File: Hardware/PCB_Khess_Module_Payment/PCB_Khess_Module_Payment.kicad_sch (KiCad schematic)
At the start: 50 parts, among them IC1 SI4435DDY-T1-GE3, IC2 MCP73844-840I_MS, J1 Conn_02x20_Odd_Even, J2 Conn_01x02, J3 Conn_01x08, J4 Conn_01x04, J6 Conn_01x08, J7 694001, U2 FSV330AF, U3 171013801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

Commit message: review schematics
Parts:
- removed U4: LM393, symbol Comparator:LM393
- added U1: MCP6001-OT, Package_TO_SOT_SMD:SOT-23-5, symbol Amplifier_Operational:MCP6001-OT
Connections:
- net +3.3V: now also U1.5 (V+)
- net Batterie_Faible_GPIO: now also U1.1
- net GND: now also U1.2 (V-)
- net Niveau_Batterie: now also U1.3 (+)
- net at R7.2, R8.1: now also U1.4 (-)

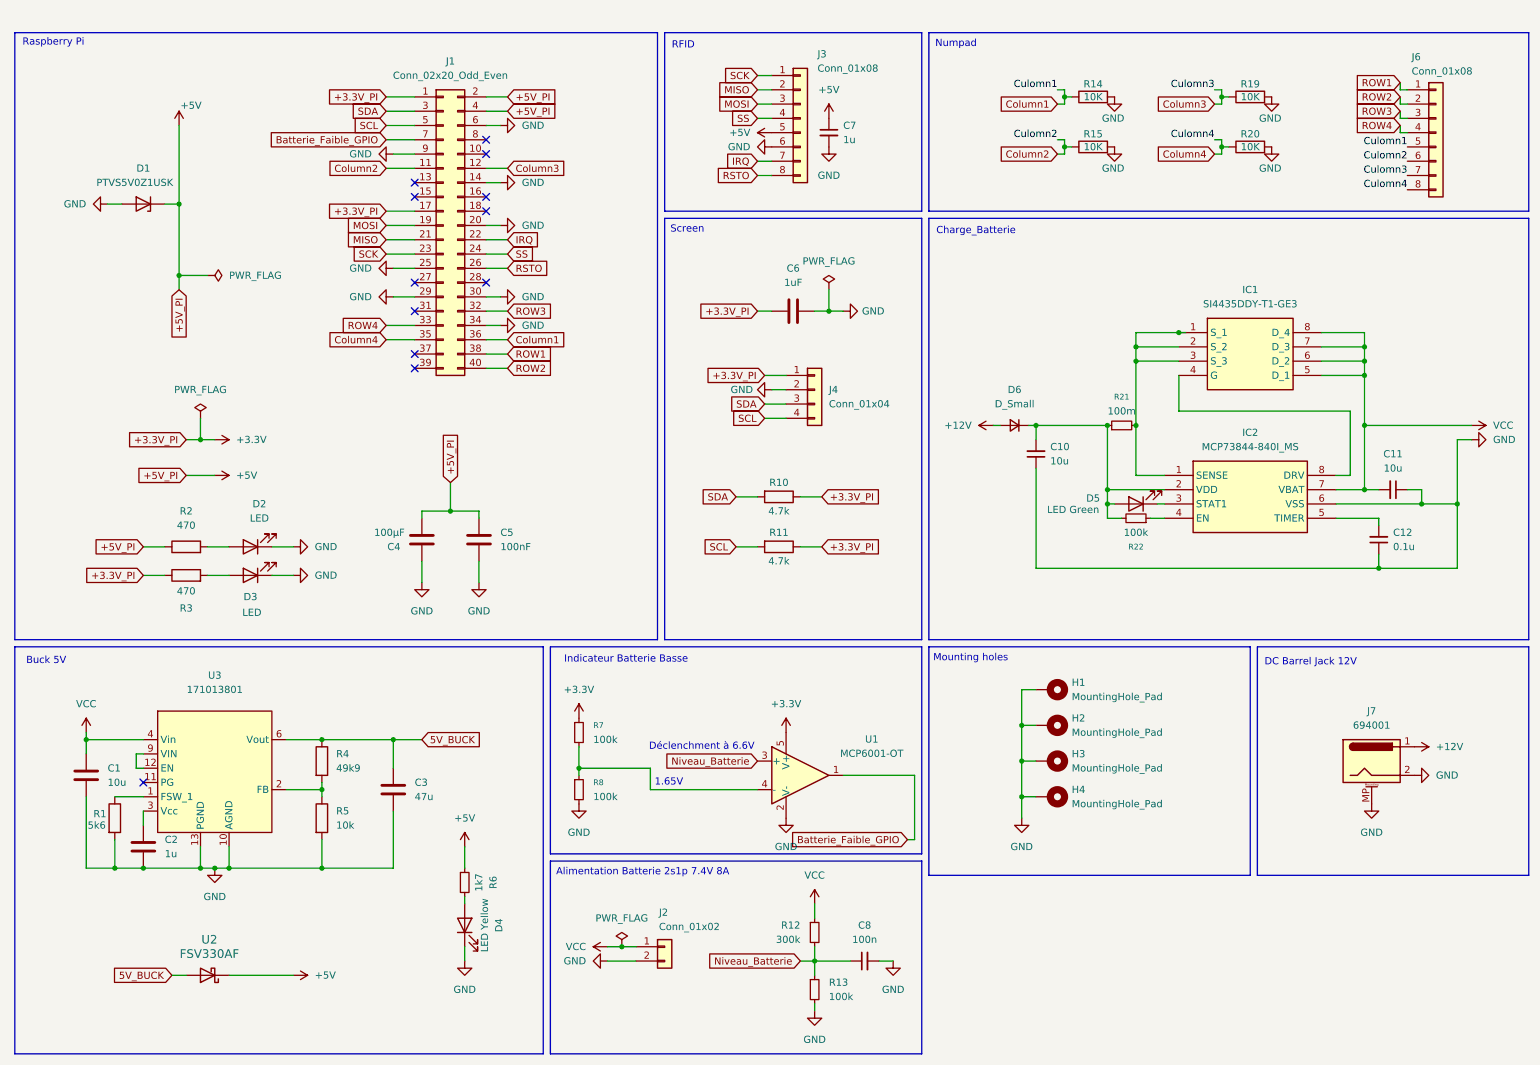
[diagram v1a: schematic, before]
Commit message: fix: update schematic
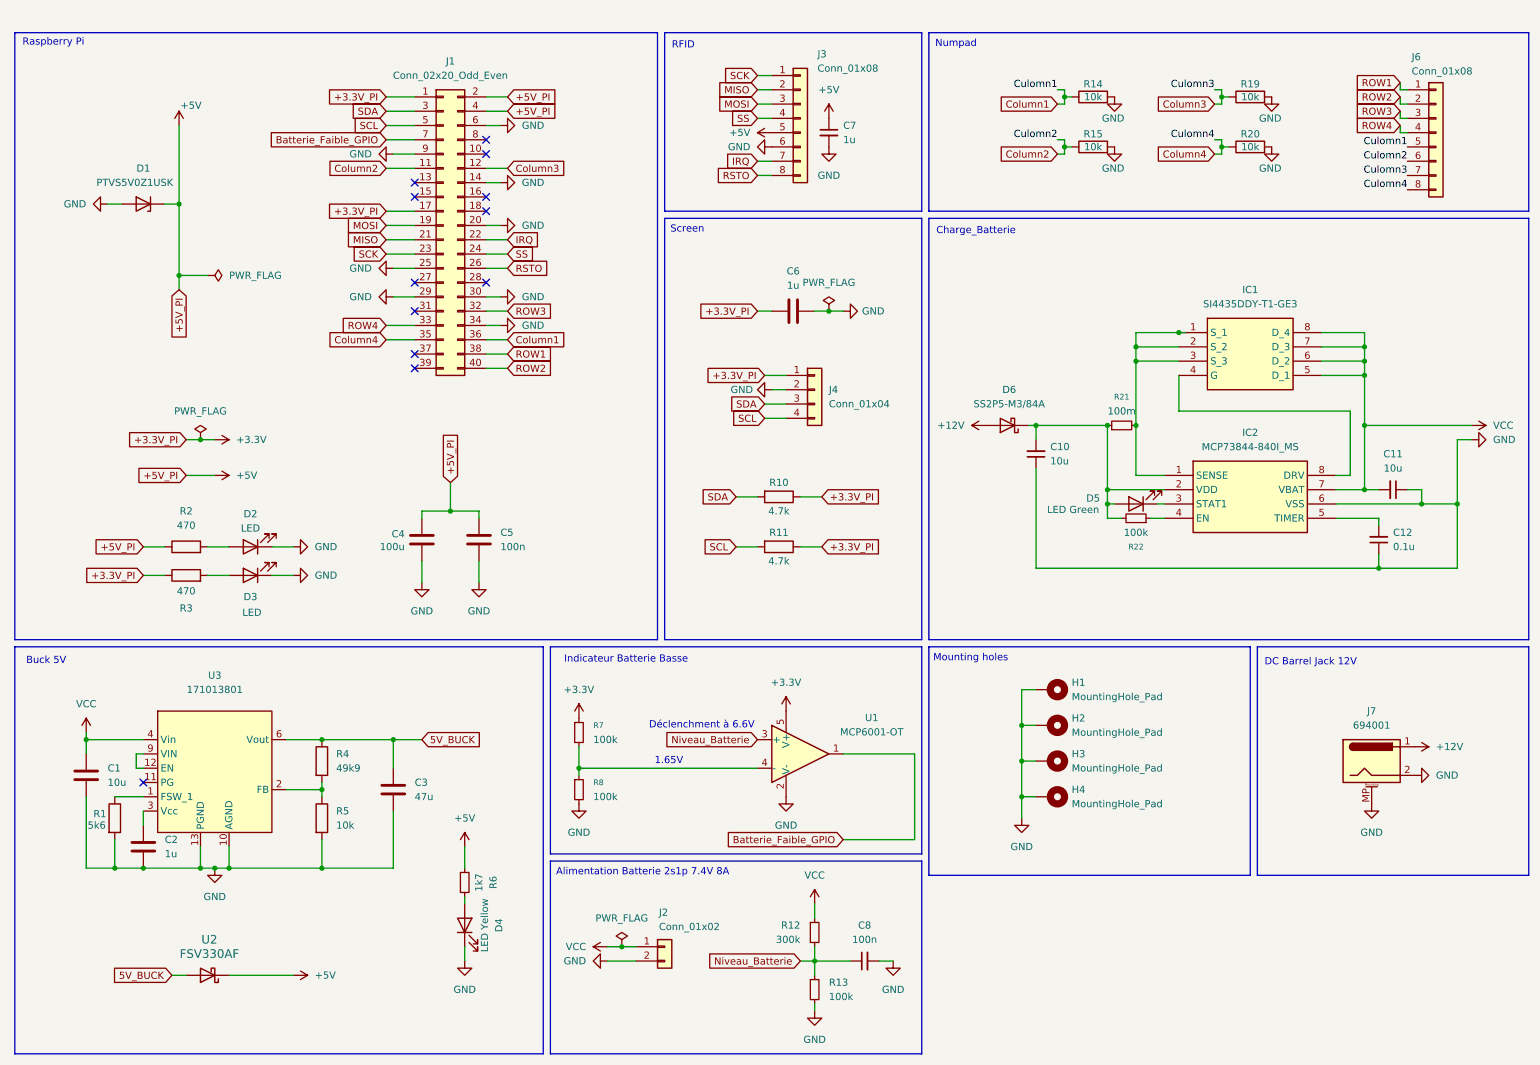
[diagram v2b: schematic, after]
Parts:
- removed D6: D_Small, symbol Device:D_Small
- added D6: SS2P5-M3/84A, Diode_SMD:D_SMP_DO-220AA, symbol Diode:SS22
- C4: value 100µF -> 100u
- C5: value 100nF -> 100n
- C6: value 1uF -> 1u
- R14, R15, R19, R20: value 10K -> 10k
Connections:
- net +12V: now also D6.2 (A)
- net at C10.2, D5.2 (A), IC2.2 (VDD)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: now also D6.1 (K)
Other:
- moved on the sheet: U1

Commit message: fix: update schematic with footprint
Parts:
- C1, C2, C6, C7: footprint Capacitor_SMD:C_0603_1608Metric_Pad1.08x0.95mm_HandSolder -> Capacitor_SMD:CP_Elec_4x5.4
- C10, C11: footprint (none) -> Capacitor_SMD:CP_Elec_4x5.4
- C12: value 0.1u -> 100n; footprint (none) -> Capacitor_SMD:C_0402_1005Metric
- C3: footprint Capacitor_SMD:C_0603_1608Metric_Pad1.08x0.95mm_HandSolder -> Capacitor_SMD:C_0805_2012Metric
- C4: footprint Capacitor_SMD:C_0603_1608Metric_Pad1.08x0.95mm_HandSolder -> Capacitor_SMD:CP_Elec_6.3x7.7
- C5, C8: footprint Capacitor_SMD:C_0603_1608Metric_Pad1.08x0.95mm_HandSolder -> Capacitor_SMD:C_0402_1005Metric
- D1: value PTVS5V0Z1USK -> 824 500 500; footprint Diode_SMD:Nexperia_DSN1608-2_1.6x0.8mm -> Diode_SMD:D_SMA
- D2, D3: footprint LED_SMD:LED_0603_1608Metric_Pad1.05x0.95mm_HandSolder -> LED_SMD:LED_0603_1608Metric
- R1, R14, R15, R19, R2, R20, R3, R5: footprint Resistor_SMD:R_0603_1608Metric_Pad0.98x0.95mm_HandSolder -> Resistor_SMD:R_0805_2012Metric
- R10, R11, R12, R13: footprint Resistor_SMD:R_0603_1608Metric_Pad0.98x0.95mm_HandSolder -> Resistor_SMD:R_0402_1005Metric
- R21: footprint (none) -> Resistor_SMD:R_1206_3216Metric
- R22: footprint (none) -> Resistor_SMD:R_0805_2012Metric
- R4: footprint Resistor_SMD:R_0603_1608Metric_Pad0.98x0.95mm_HandSolder -> Resistor_SMD:R_0603_1608Metric
- R6: value 1k7 -> 1k5; footprint Resistor_SMD:R_0603_1608Metric_Pad0.98x0.95mm_HandSolder -> Resistor_SMD:R_0805_2012Metric
- R7, R8: footprint (none) -> Resistor_SMD:R_0402_1005Metric
- U2: value FSV330AF -> FSV340AF; footprint Diode_SMD:D_SOD-123 -> Diode_SMD:D_SMC
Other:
- moved on the sheet: C4, C5, C7, D1, U2

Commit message: fix: update schematic and footprint
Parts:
- removed J7: 694001, Connector_BarrelJack:BarrelJack_Wuerth_6941xx301002, symbol Connector:Barrel_Jack_MountingPin
- added J5: 694106301002, Connector_BarrelJack:BarrelJack_Wuerth_694106106102_2.0x5.5mm, symbol Connector:Barrel_Jack_Switch
- U3: footprint Package_DFN_QFN:QFN-16-1EP_3x3mm_P0.5mm_EP1.9x1.9mm -> LIB_171013801:171013801
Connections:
- net +12V: now also J5.1
- net GND: now also J5.2
- no-connect marks 12 -> 13

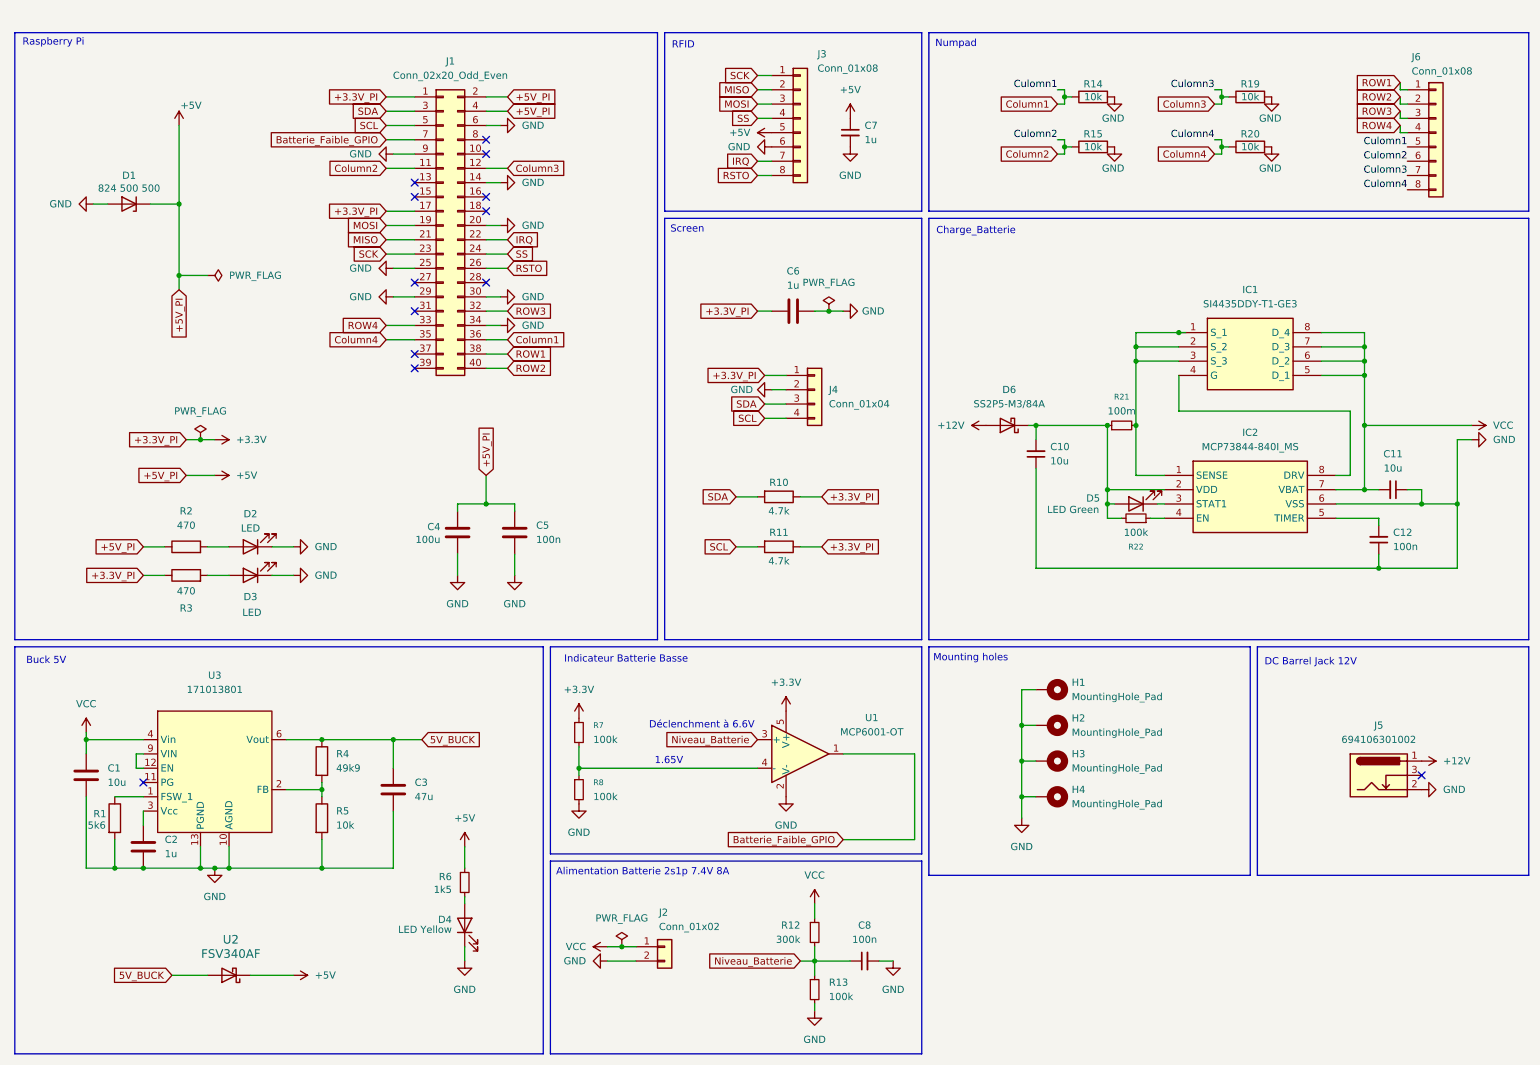
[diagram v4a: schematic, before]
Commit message: feat: suply via shield
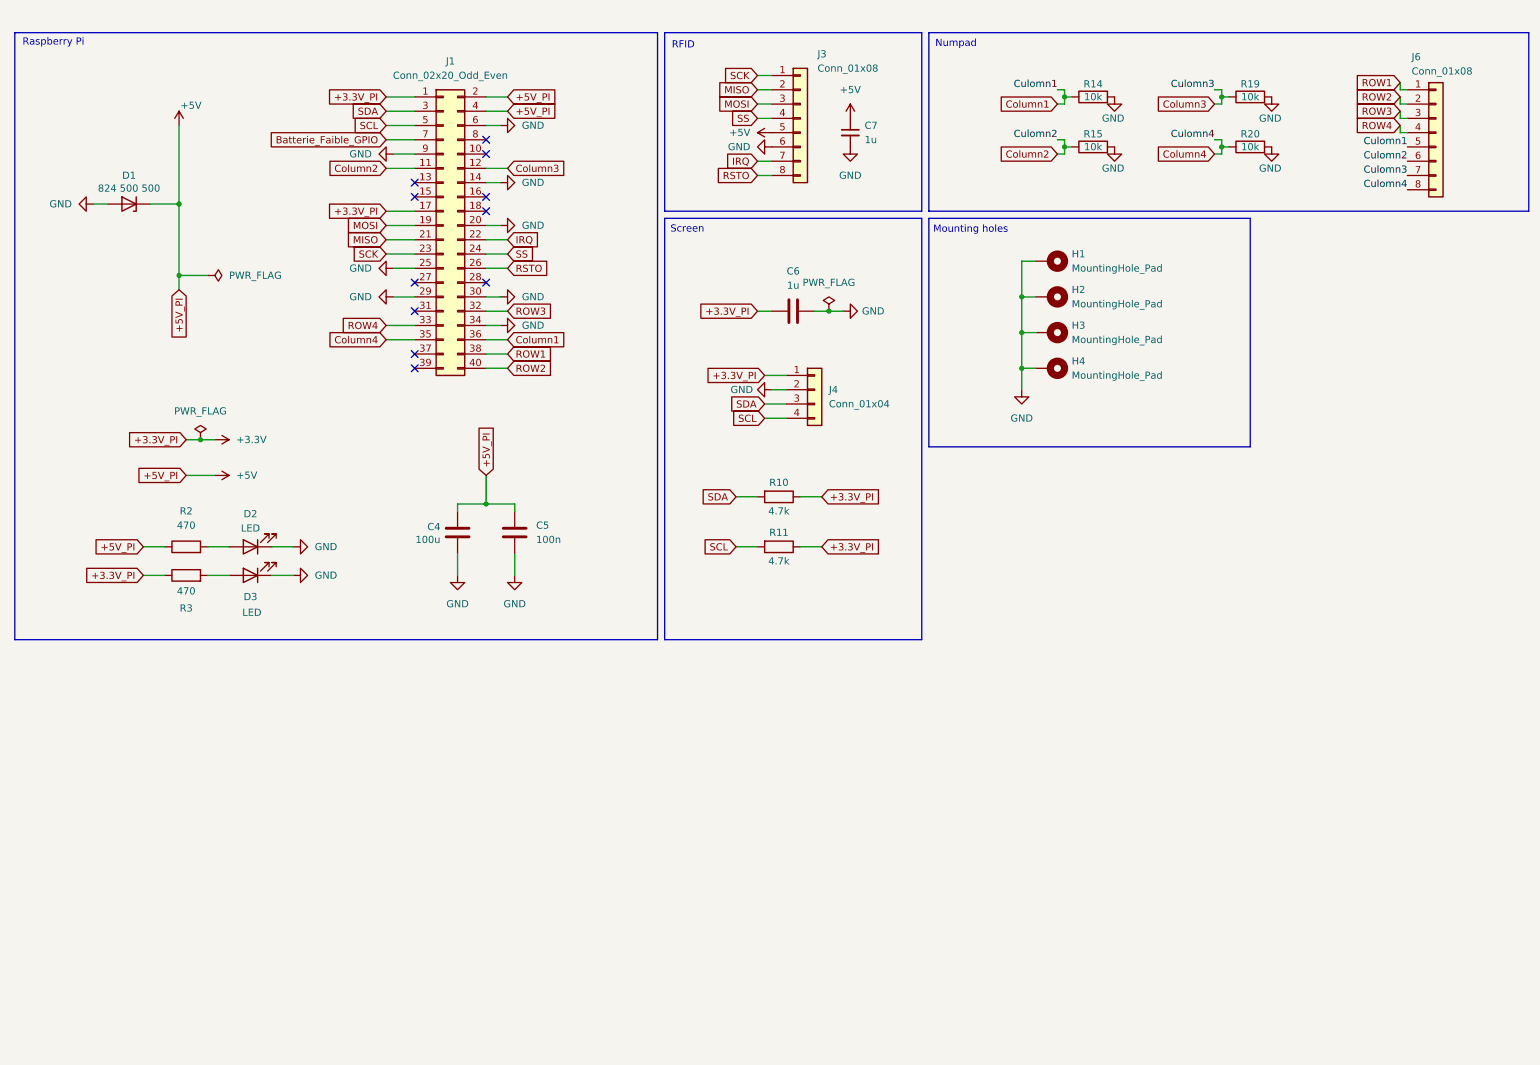
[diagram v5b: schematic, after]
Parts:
- removed C1: 10u, Capacitor_SMD:CP_Elec_4x5.4, symbol Device:C
- removed C10, C11: 10u, Capacitor_SMD:CP_Elec_4x5.4, symbol Device:C_Small
- removed C12, C8: 100n, Capacitor_SMD:C_0402_1005Metric, symbol Device:C_Small
- removed C2: 1u, Capacitor_SMD:CP_Elec_4x5.4, symbol Device:C
- removed C3: 47u, Capacitor_SMD:C_0805_2012Metric, symbol Device:C
- removed D4: LED Yellow, LED_SMD:LED_0603_1608Metric, symbol Device:LED
- removed D5: LED Green, LED_SMD:LED_0603_1608Metric, symbol Device:LED
- removed D6: SS2P5-M3/84A, Diode_SMD:D_SMP_DO-220AA, symbol Diode:SS22
- removed IC1: SI4435DDY-T1-GE3, SI4435DDY-T1-GE3:SOIC127P600X175-8N, symbol SI4435DDY-T1-GE3:SI4435DDY-T1-GE3
- removed IC2: MCP73844-840I_MS, MCP73844-840I_MS:SOP65P490X110-8N, symbol MCP73844-840I_MS:MCP73844-840I_MS
- removed J2: Conn_01x02, Connector_JST:JST_XA_S02B-XASK-1_1x02_P2.50mm_Horizontal, symbol Connector_Generic:Conn_01x02
- removed J5: 694106301002, Connector_BarrelJack:BarrelJack_Wuerth_694106106102_2.0x5.5mm, symbol Connector:Barrel_Jack_Switch
- removed R1: 5k6, Resistor_SMD:R_0805_2012Metric, symbol Device:R
- removed R12: 300k, Resistor_SMD:R_0402_1005Metric, symbol Device:R_Small
- removed R13, R7, R8: 100k, Resistor_SMD:R_0402_1005Metric, symbol Device:R_Small
- removed R21: 100m, Resistor_SMD:R_1206_3216Metric, symbol Device:R_Small
- removed R22: 100k, Resistor_SMD:R_0805_2012Metric, symbol Device:R_Small
- removed R4: 49k9, Resistor_SMD:R_0603_1608Metric, symbol Device:R
- removed R5: 10k, Resistor_SMD:R_0805_2012Metric, symbol Device:R
- removed R6: 1k5, Resistor_SMD:R_0805_2012Metric, symbol Device:R_Small
- removed U1: MCP6001-OT, Package_TO_SOT_SMD:SOT-23-5, symbol Amplifier_Operational:MCP6001-OT
- removed U2: FSV340AF, Diode_SMD:D_SMC, symbol Device:D_Schottky
- removed U3: 171013801, LIB_171013801:171013801, symbol Wurth_regulator_171013801:Regulator_Wurth_171013801
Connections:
- no-connect marks 13 -> 11
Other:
- note removed: "1.65V"
- note removed: "Alimentation Batterie 2s1p 7.4V 8A"
- note removed: "Buck 5V"
- note removed: "Charge_Batterie"
- note removed: "DC Barrel Jack 12V"
- note removed: "Déclenchment à 6.6V"
- note removed: "Indicateur Batterie Basse"
- moved on the sheet: H1, H2, H3, H4
